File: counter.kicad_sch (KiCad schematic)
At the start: 39 parts, among them J1 Eurorack Power, J2 Clock In 1, J3 Reset In 1, J4 Clock In 2, J5 Reset In 2, Q1 2N3904, Q2 2N3904, SW1 Reset 1, SW2 Reset 2, U1 LM7805_TO220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

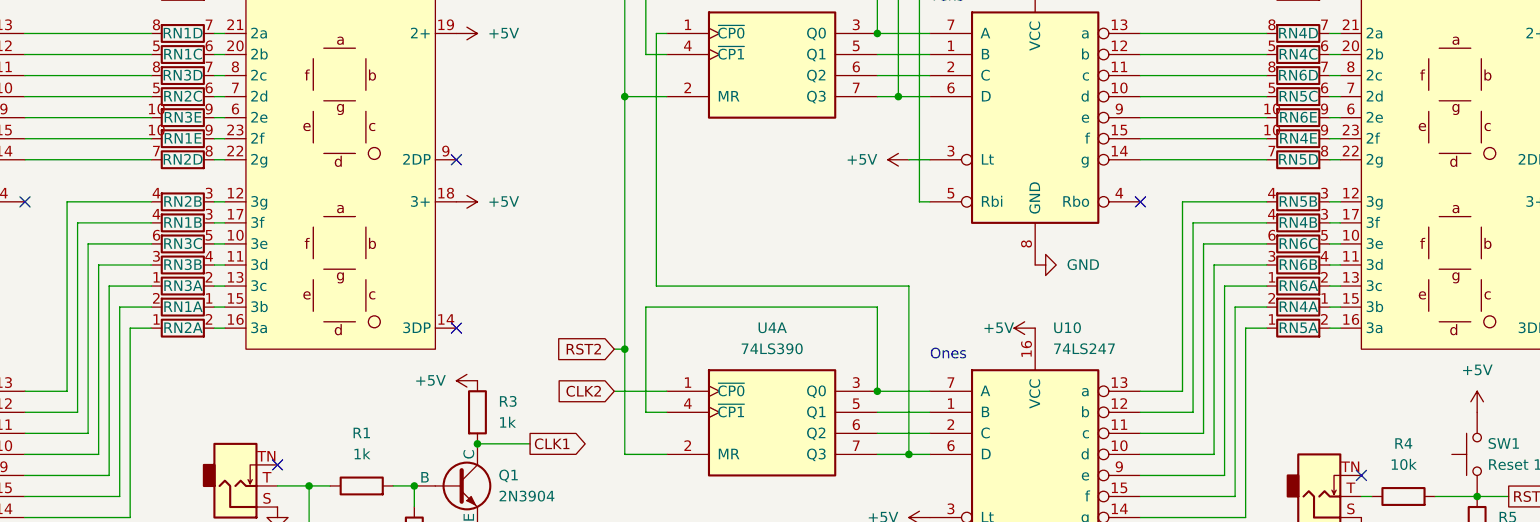
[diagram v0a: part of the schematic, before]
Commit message: Fix ones place digit being backwards
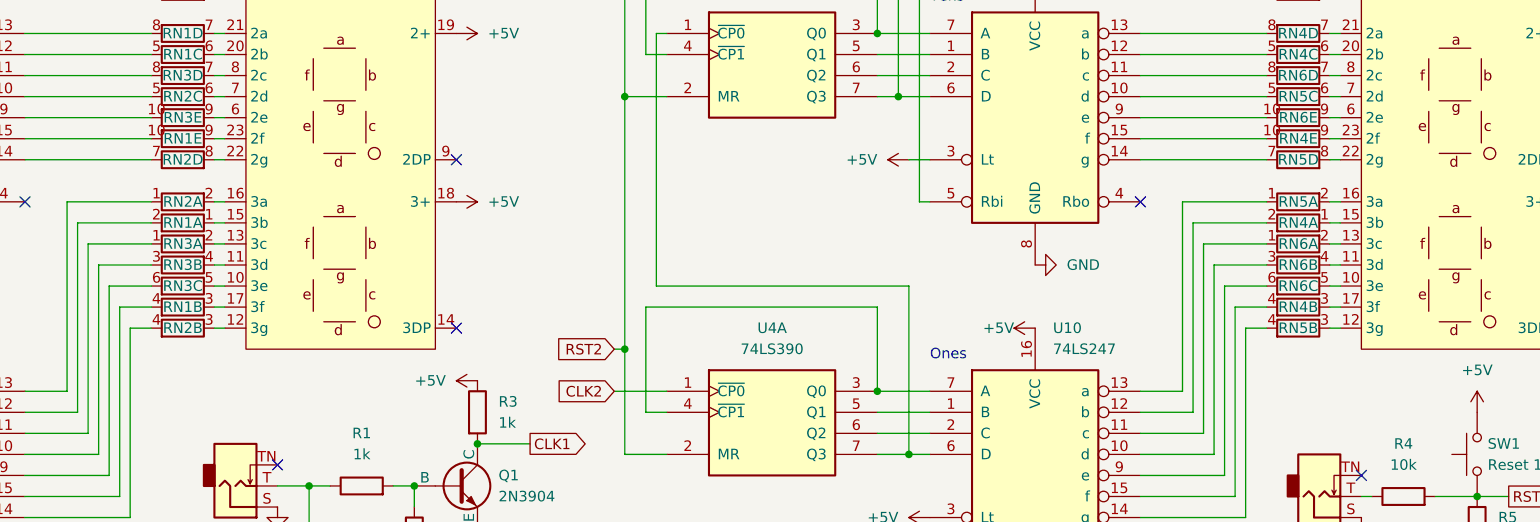
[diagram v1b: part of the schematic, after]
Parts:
- D1, D2: symbol ba56-11surkwa:ba56-11surkwa -> MAI_Display_Character:BA56-11xxWA
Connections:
- net at RN6.6 (R3.2): now also U10.9 (e); no longer U10.11 (c)
- net at RN5.1 (R1.1): now also U10.13 (a); no longer U10.14 (g)
- net at RN6.1 (R1.1): now also U10.11 (c); no longer U10.9 (e)
- net at RN2.4 (R2.2): now also U7.14 (g); no longer U7.13 (a)
- net at RN3.6 (R3.2): now also U7.9 (e); no longer U7.11 (c)
- net at U7.12 (b): now also RN1.2 (R1.2); no longer RN1.4 (R2.2)
- net at RN2.1 (R1.1): now also U7.13 (a); no longer U7.14 (g)
- net at U7.15 (f): now also RN1.4 (R2.2); no longer RN1.2 (R1.2)
- net at RN3.1 (R1.1): now also U7.11 (c); no longer U7.9 (e)
- net at U10.12 (b): now also RN4.2 (R1.2); no longer RN4.4 (R2.2)
- net at RN5.4 (R2.2): now also U10.14 (g); no longer U10.13 (a)
- net at U10.15 (f): now also RN4.4 (R2.2); no longer RN4.2 (R1.2)
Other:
- moved on the sheet: RN1A, RN1B, RN2A, RN2B, RN3A, RN3C, RN4A, RN4B, RN5A, RN5B, RN6A, RN6C

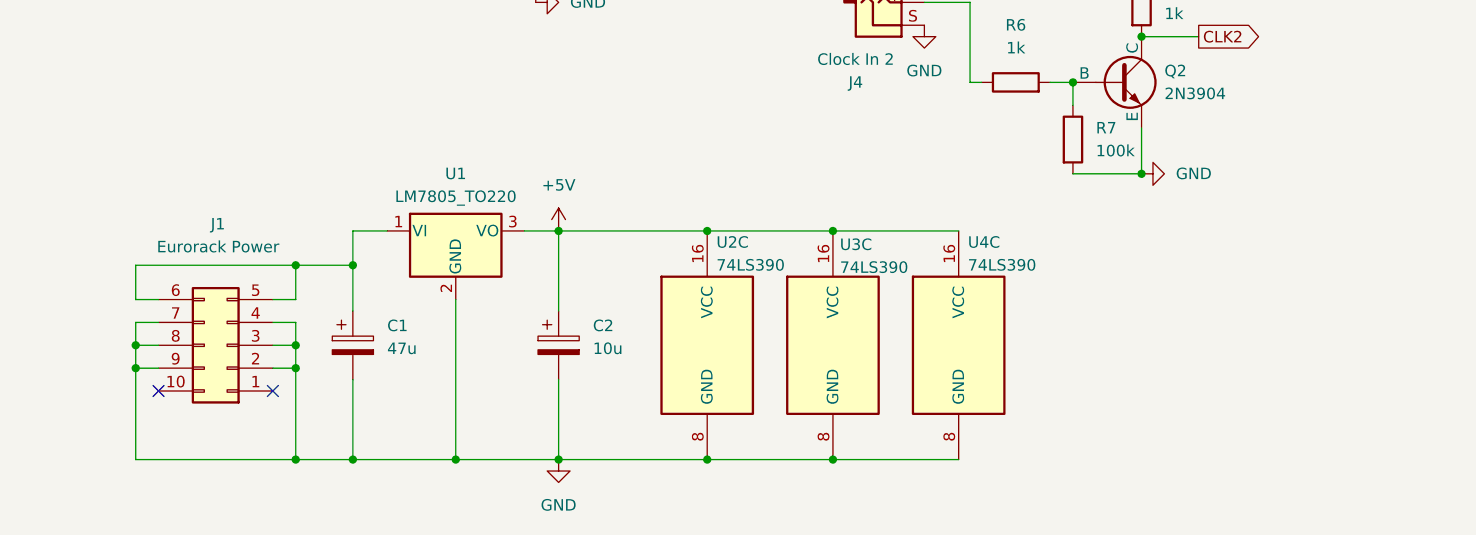
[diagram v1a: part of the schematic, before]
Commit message: Add diodes to reduce regulator input voltage
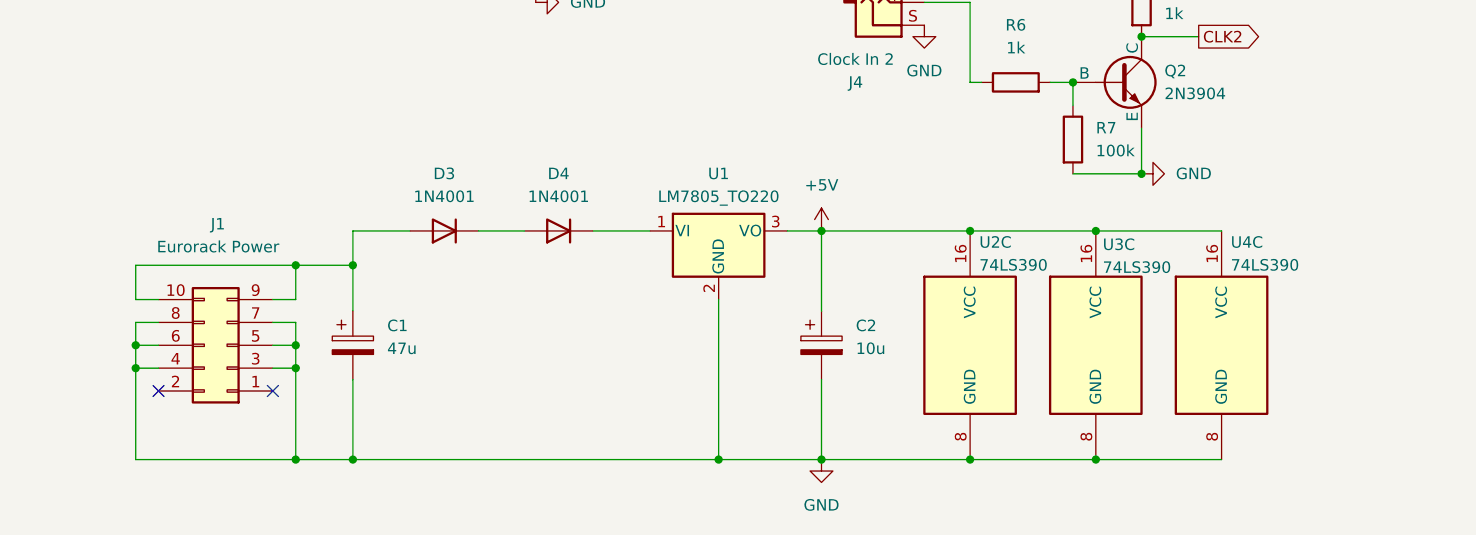
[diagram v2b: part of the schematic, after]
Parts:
- added D3, D4: 1N4001, Diode_THT:D_DO-41_SOD81_P10.16mm_Horizontal, symbol Diode:1N4001
- J1: symbol Connector_Generic:Conn_02x05_Counter_Clockwise -> Connector_Generic:Conn_02x05_Odd_Even
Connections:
- net GND: now also J1.5 (Pin_5), J1.6 (Pin_6); no longer J1.2 (Pin_2), J1.9 (Pin_9)
- net at J1.10 (Pin_10): now also C1.1, J1.9 (Pin_9), D3.2 (A)
- new net: D4.1 (K), U1.1 (VI)
- new net: D3.1 (K), D4.2 (A)
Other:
- moved on the sheet: C2, U1, U2C, U3C, U4C

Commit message: Rev. 2
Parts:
- added H1: MountingHole, MountingHole:MountingHole_4.3mm_M4, symbol Mechanical:MountingHole
- C1: footprint Capacitor_THT:CP_Radial_D6.3mm_P2.50mm -> Capacitor_THT:CP_Radial_D5.0mm_P2.00mm
- R1, R6: value 1k -> 10k
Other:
- note added: "10k"
- note added: "1k"
